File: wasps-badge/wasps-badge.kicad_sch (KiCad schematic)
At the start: 25 parts, among them J1 Conn_Debug, J2 Conn_AddOn, J3 Conn_CTF, J4 Conn_Misc, SW1 SW_SPST, SW2 SW_Push, SW3 SW_Push, U1 CH32V003FxPx

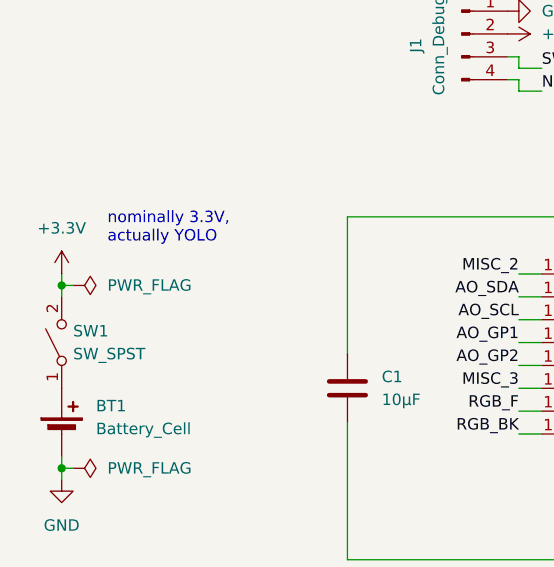
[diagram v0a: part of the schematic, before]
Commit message: Add missing footprint assignments
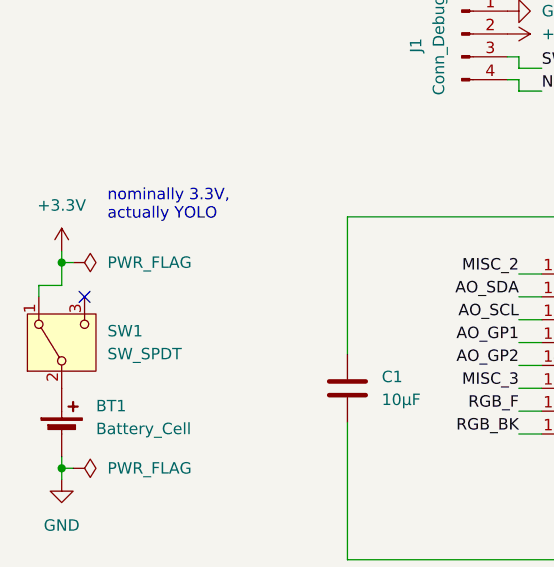
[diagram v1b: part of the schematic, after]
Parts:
- removed SW1: SW_SPST, symbol Switch:SW_SPST
- added SW1: SW_SPDT, CustomLibrary:SW_SPDT_MSS22D18_SMD, symbol Switch:SW_SPDT
- SW2, SW3: footprint (none) -> CustomLibrary:SW_PUSH_L4.0-W3.0-LS5.0_SMD
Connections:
- net +3.3V: now also SW1.1 (A)
- net at BT1.1 (+): now also SW1.2 (B)
- no-connect marks 4 -> 5
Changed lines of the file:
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@@
 	(text "nominally 3.3V,\nactually YOLO"
 		(exclude_from_sim no)
-		(at 43.18 58.42 0)
+		(at 43.18 55.88 0)
 		(effects
 			(font
@@
 	)
 	(junction
-		(at 38.1 64.77)
+		(at 38.1 62.23)
 		(diameter 0)
 		(color 0 0 0 0)
@@
 	)
 	(no_connect
+		(at 40.64 66.04)
+	)
+	(no_connect
 		(at 204.47 63.5)
 	)
@@
 	(wire
 		(pts
+			(xy 35.56 66.04) (xy 35.56 64.77)
+		)
+		(stroke
+			(width 0)
+			(type default)
+		)
+	)
+	(wire
+		(pts
 			(xy 157.48 38.1) (xy 158.75 38.1)
 		)
@@
 	(wire
 		(pts
-			(xy 38.1 64.77) (xy 38.1 66.04)
+			(xy 38.1 62.23) (xy 38.1 64.77)
 		)
 		(stroke
@@
 	(wire
 		(pts
+			(xy 35.56 64.77) (xy 38.1 64.77)
+		)
+		(stroke
+			(width 0)
+			(type default)
+		)
+	)
+	(wire
+		(pts
 			(xy 101.6 95.25) (xy 101.6 93.98)
 		)
@@
 	(wire
 		(pts
-			(xy 38.1 63.5) (xy 38.1 64.77)
+			(xy 38.1 60.96) (xy 38.1 62.23)
 		)
 		(stroke
@@
 	(wire
 		(pts
-			(xy 39.37 64.77) (xy 38.1 64.77)
+			(xy 39.37 62.23) (xy 38.1 62.23)
 		)
 		(stroke
@@
 	(symbol
 		(lib_id "power:+3.3V")
-		(at 38.1 63.5 0)
+		(at 38.1 60.96 0)
 		(unit 1)
 		(exclude_from_sim no)
@@
 		(fields_autoplaced yes)
 		(property "Reference" "#PWR04"
-			(at 38.1 67.31 0)
+			(at 38.1 64.77 0)
 			(effects
 				(font
@@
 		)
 		(property "Value" "+3.3V"
-			(at 38.1 58.42 0)
+			(at 38.1 55.88 0)
 			(effects
 				(font
@@
 		)
 		(property "Footprint" ""
-			(at 38.1 63.5 0)
+			(at 38.1 60.96 0)
 			(effects
 				(font
@@
 		)
 		(property "Datasheet" ""
-			(at 38.1 63.5 0)
+			(at 38.1 60.96 0)
 			(effects
 				(font
@@
 		)
 		(property "Description" "Power symbol creates a global label with name \"+3.3V\""
-			(at 38.1 63.5 0)
+			(at 38.1 60.96 0)
 			(effects
 				(font
@@
 	(symbol
 		(lib_id "power:PWR_FLAG")
-		(at 39.37 64.77 270)
+		(at 39.37 62.23 270)
 		(unit 1)
 		(exclude_from_sim no)
@@
 		(fields_autoplaced yes)
 		(property "Reference" "#FLG01"
-			(at 41.275 64.77 0)
+			(at 41.275 62.23 0)
 			(effects
 				(font
@@
 		)
 		(property "Value" "PWR_FLAG"
-			(at 43.18 64.7699 90)
+			(at 43.18 62.2299 90)
 			(effects
 				(font
@@
 		)
 		(property "Footprint" ""
-			(at 39.37 64.77 0)
+			(at 39.37 62.23 0)
 			(effects
 				(font
@@
 		)
 		(property "Datasheet" "~"
-			(at 39.37 64.77 0)
+			(at 39.37 62.23 0)
 			(effects
 				(font
@@
 		)
 		(property "Description" "Special symbol for telling ERC where power comes from"
-			(at 39.37 64.77 0)
+			(at 39.37 62.23 0)
 			(effects
 				(font
@@
 	)
 	(symbol
+		(lib_id "Switch:SW_SPDT")
+		(at 38.1 71.12 90)
+		(unit 1)
+		(exclude_from_sim no)
+		(in_bom yes)
+		(on_board yes)
+		(dnp no)
+		(fields_autoplaced yes)
+		(property "Reference" "SW1"
+			(at 43.18 69.8499 90)
+			(effects
+				(font
+					(size 1.27 1.27)
+				)
+				(justify right)
+			)
+		)
+		(property "Value" "SW_SPDT"
+			(at 43.18 72.3899 90)
+			(effects
+				(font
+					(size 1.27 1.27)
+				)
+				(justify right)
+			)
+		)
+		(property "Footprint" "CustomLibrary:SW_SPDT_MSS22D18_SMD"
+			(at 38.1 71.12 0)
+			(effects
+				(font
+					(size 1.27 1.27)
+				)
+				(hide yes)
+			)
+		)
+		(property "Datasheet" "~"
+			(at 45.72 71.12 0)
+			(effects
+				(font
+					(size 1.27 1.27)
+				)
+				(hide yes)
+			)
+		)
+		(property "Description" "Switch, single pole double throw"
+			(at 38.1 71.12 0)
+			(effects
+				(font
+					(size 1.27 1.27)
+				)
+				(hide yes)
+			)
+		)
+		(pin "1"
+		)
+		(pin "3"
+		)
+		(pin "2"
+		)
+		(instances
+			(project ""
+				(path "/d84c9b78-3f5c-4638-8181-576e3884c024"
+					(reference "SW1")
+					(unit 1)
+				)
+			)
+		)
+	)
+	(symbol
 		(lib_id "power:+3.3V")
 		(at 87.63 36.83 270)
@@
 			)
 		)
-		(property "Footprint" ""
+		(property "Footprint" "CustomLibrary:SW_PUSH_L4.0-W3.0-LS5.0_SMD"
 			(at 132.08 87.63 0)
 			(effects
@@
 			)
 		)
-		(property "Footprint" ""
+		(property "Footprint" "CustomLibrary:SW_PUSH_L4.0-W3.0-LS5.0_SMD"
 			(at 259.08 106.68 0)
 			(effects
@@
 					(unit 1)
 				)
-			)
-		)
-	)
-	(symbol
-		(lib_id "Switch:SW_SPST")
-		(at 38.1 71.12 90)
-		(unit 1)
-		(exclude_from_sim no)
-		(in_bom yes)
-		(on_board yes)
-		(dnp no)
-		(fields_autoplaced yes)
-		(property "Reference" "SW1"
-			(at 39.37 69.8499 90)
-			(effects
-				(font
-					(size 1.27 1.27)
-				)
-				(justify right)
-			)
-		)
-		(property "Value" "SW_SPST"
-			(at 39.37 72.3899 90)
-			(effects
-				(font
-					(size 1.27 1.27)
-				)
-				(justify right)
-			)
-		)
-		(property "Footprint" ""
-			(at 38.1 71.12 0)
-			(effects
-				(font
-					(size 1.27 1.27)
-				)
-				(hide yes)
-			)
-		)
-		(property "Datasheet" "~"
-			(at 38.1 71.12 0)
-			(effects
-				(font
-					(size 1.27 1.27)
-				)
-				(hide yes)
-			)
-		)
-		(property "Description" "Single Pole Single Throw (SPST) switch"
-			(at 38.1 71.12 0)
-			(effects
-				(font
-					(size 1.27 1.27)
-				)
-				(hide yes)
-			)
-		)
-		(pin "2"
-		)
-		(pin "1"
-		)
-		(instances
-			(project ""
-				(path "/d84c9b78-3f5c-4638-8181-576e3884c024"
-					(reference "SW1")
-					(unit 1)
-				)

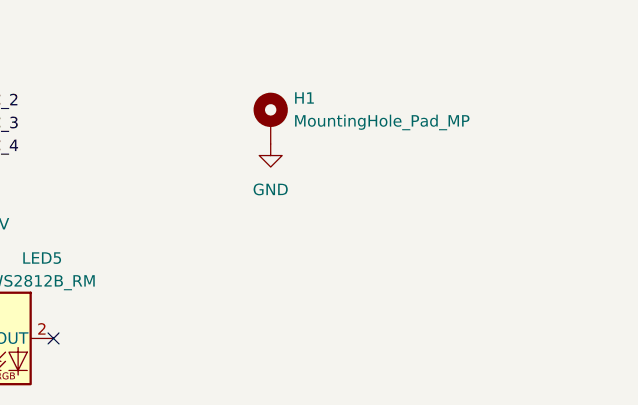
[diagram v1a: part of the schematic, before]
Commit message: Change mounting hole pad name
The footprint calls it "1", so "1" it is.
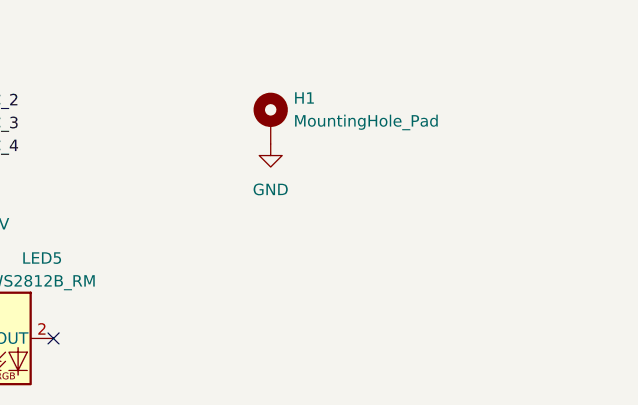
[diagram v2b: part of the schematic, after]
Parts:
- H1: value MountingHole_Pad_MP -> MountingHole_Pad; symbol Mechanical:MountingHole_Pad_MP -> Mechanical:MountingHole_Pad
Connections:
- net GND: now also H1.1; no longer H1.MP
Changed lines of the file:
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@@
 	)
 	(symbol
-		(lib_id "Mechanical:MountingHole_Pad_MP")
+		(lib_id "Mechanical:MountingHole_Pad")
 		(at 228.6 39.37 0)
 		(unit 1)
@@
 			)
 		)
-		(property "Value" "MountingHole_Pad_MP"
+		(property "Value" "MountingHole_Pad"
 			(at 231.14 39.3699 0)
 			(effects
@@
 			)
 		)
-		(property "Description" "Mounting Hole with connection as pad named MP"
+		(property "Description" "Mounting Hole with connection"
 			(at 228.6 39.37 0)
 			(effects
@@
 			)
 		)
-		(pin "MP"
+		(pin "1"
 		)
 		(instances

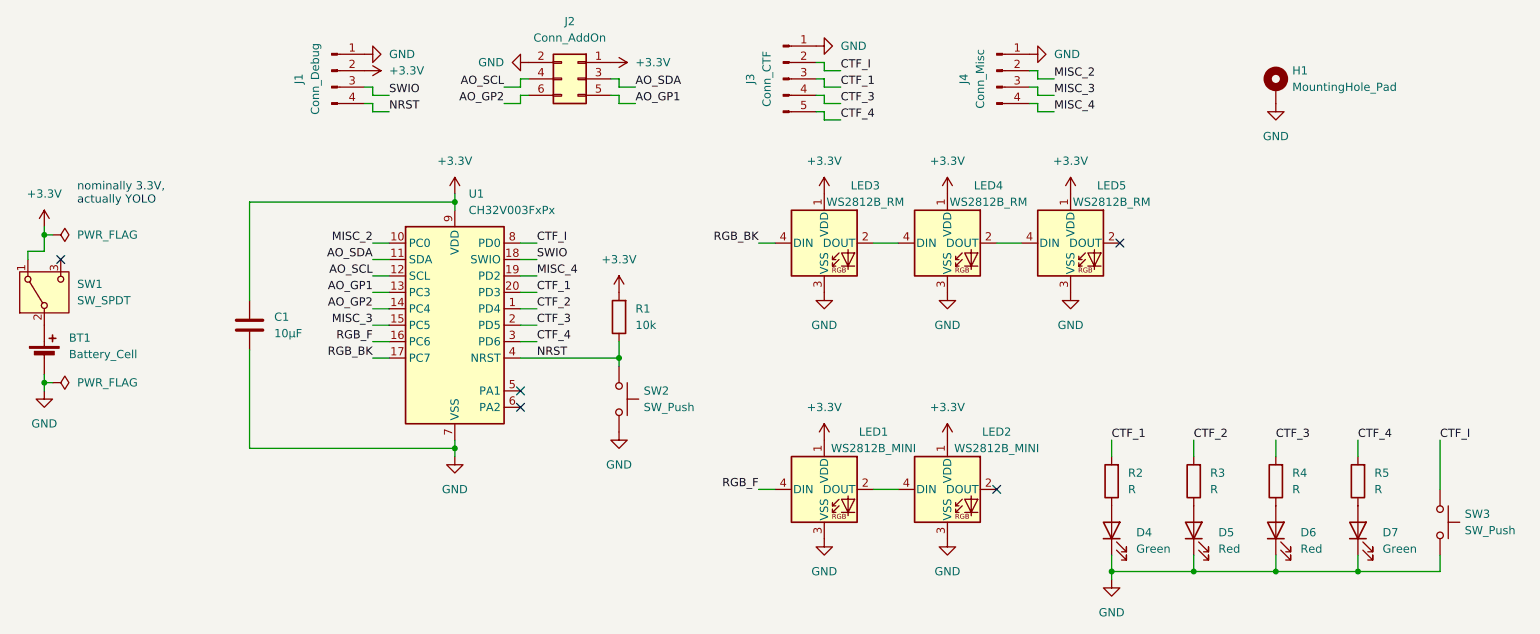
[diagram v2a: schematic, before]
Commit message: First routing attempt; drop MISC header
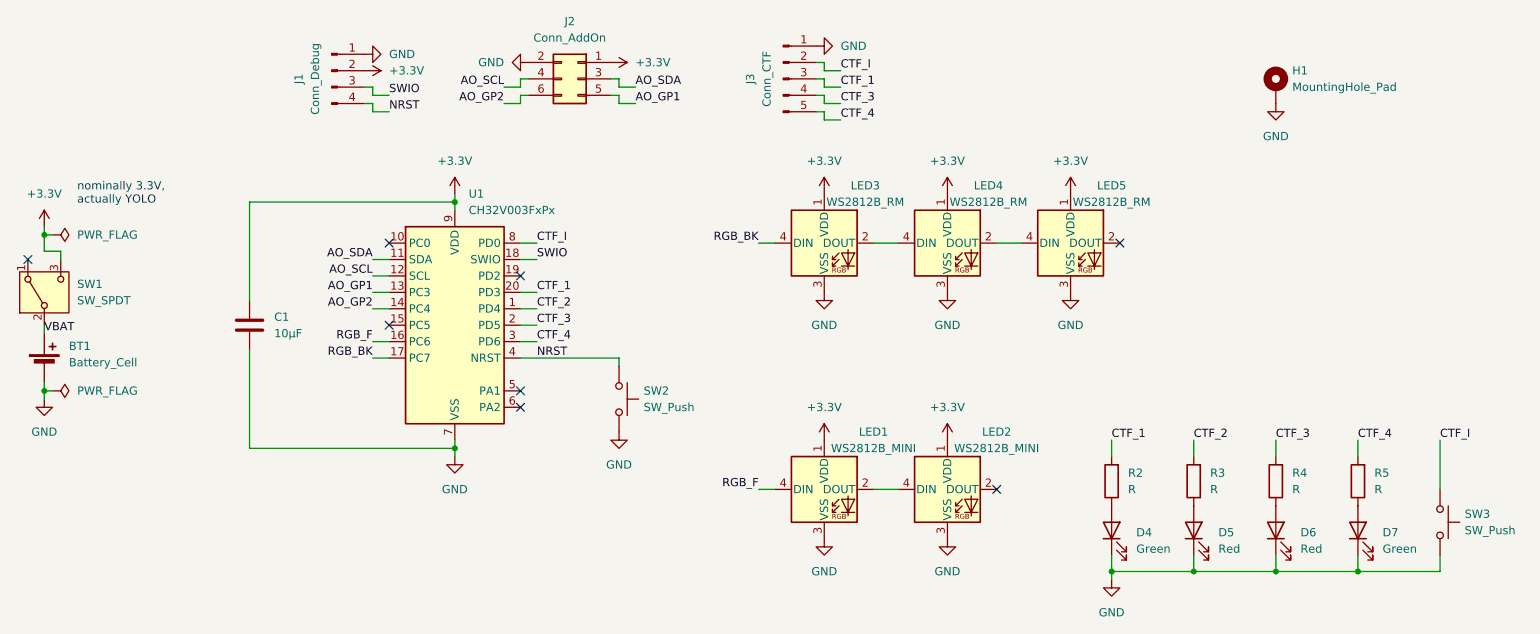
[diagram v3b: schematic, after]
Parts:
- removed J4: Conn_Misc, Connector_PinHeader_2.54mm:PinHeader_1x04_P2.54mm_Vertical, symbol Connector:Conn_01x04_Pin
- removed R1: 10k, Resistor_SMD:R_0603_1608Metric_Pad0.98x0.95mm_HandSolder, symbol Device:R
- LED3, LED4, LED5: footprint LED_SMD:LED_WS2812B_PLCC4_5.0x5.0mm_P3.2mm -> CustomLibrary:LED_WS2812B_Reverse
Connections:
- net +3.3V: now also SW1.3 (C); no longer SW1.1 (A)
- net VBAT: now reaches BT1.1 (+), SW1.2 (B)
- net MISC_2: no longer names the net of U1.10 (PC0)
- net MISC_3: no longer names the net of U1.15 (PC5)
- net MISC_4: no longer names the net of U1.19 (PD2)
- no-connect marks 5 -> 8
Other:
- moved on the sheet: BT1

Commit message: Add labeling
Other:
- company: (none) -> ${COMPANY}
- title: (none) -> ${TITLE}
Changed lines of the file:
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@@
 	(generator_version "9.0")
 	(paper "A4")
+	(title_block
+		(title "${TITLE}")
+		(date "${DATE}")
+		(rev "${REVISION}")
+		(company "${COMPANY}")
+	)
 	(text "nominally 3.3V,\nactually YOLO"
 		(exclude_from_sim no)

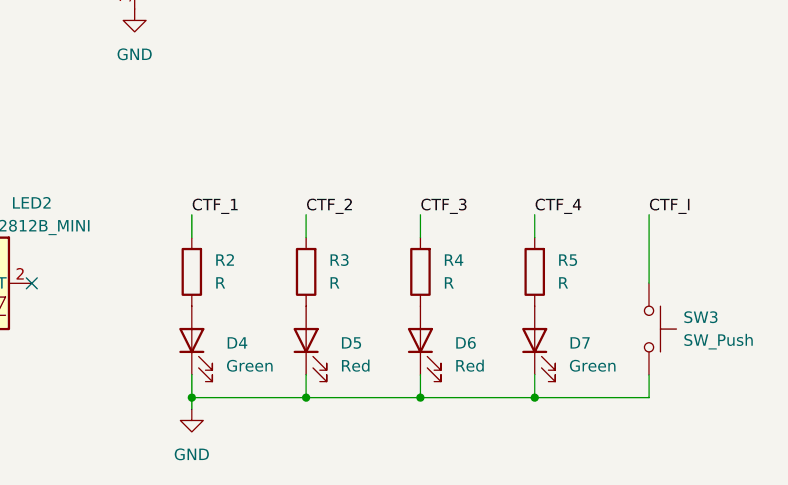
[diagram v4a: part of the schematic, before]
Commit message: Define resistor values
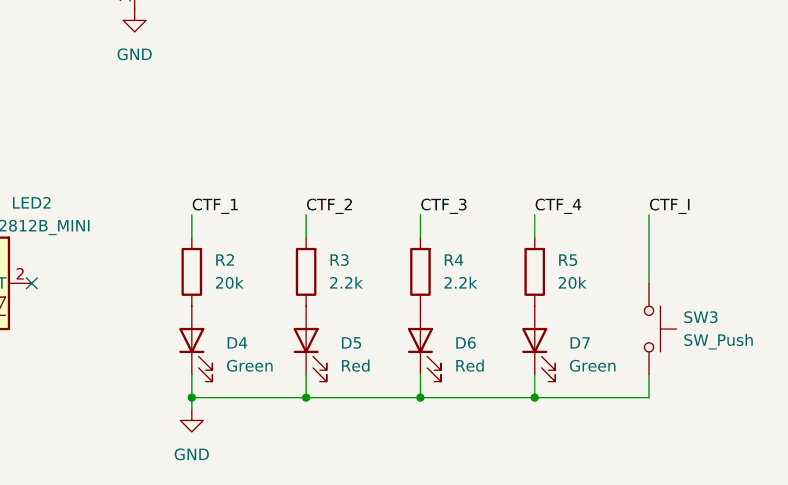
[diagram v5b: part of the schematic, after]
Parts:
- R2, R5: value R -> 20k
- R3, R4: value R -> 2.2k
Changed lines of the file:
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@@
 			)
 		)
-		(property "Value" "R"
+		(property "Value" "2.2k"
 			(at 231.14 101.5999 0)
 			(effects
@@
 			)
 		)
-		(property "Value" "R"
+		(property "Value" "20k"
 			(at 205.74 101.5999 0)
 			(effects
@@
 			)
 		)
-		(property "Value" "R"
+		(property "Value" "2.2k"
 			(at 218.44 101.5999 0)
 			(effects
@@
 			)
 		)
-		(property "Value" "R"
+		(property "Value" "20k"
 			(at 243.84 101.5999 0)
 			(effects

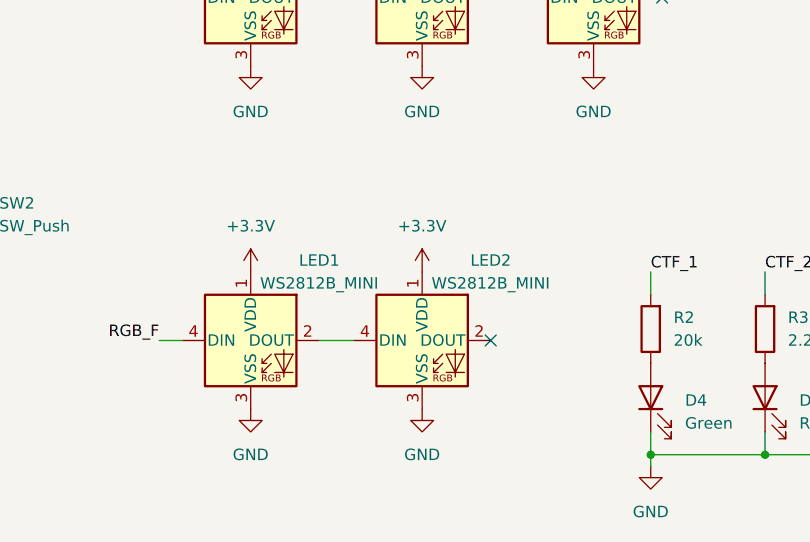
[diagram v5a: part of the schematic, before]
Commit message: Add supplier part numbers
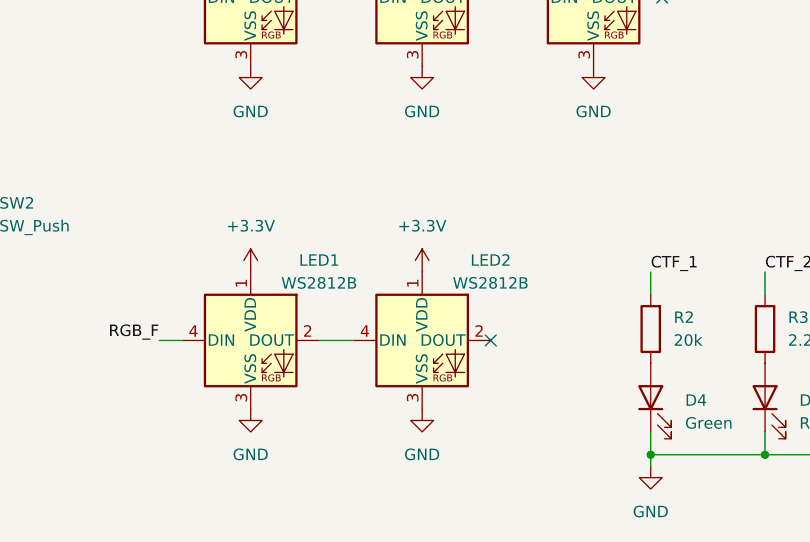
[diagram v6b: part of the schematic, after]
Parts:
- BT1: LCSC (none) -> C70377
- C1: LCSC (none) -> C19702
- D4, D7: LCSC (none) -> C12624
- D5, D6: LCSC (none) -> C965799
- J2: LCSC (none) -> C5116527
- LED1, LED2: value WS2812B_MINI -> WS2812B
- R2, R5: LCSC (none) -> C4184
- R3, R4: LCSC (none) -> C4190
- SW1: LCSC (none) -> C41375971
- SW2, SW3: LCSC (none) -> C5221275
- U1: LCSC (none) -> C5187096
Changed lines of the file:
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@@
+			)
+		)
+		(property "LCSC" "C12624"
+			(at 207.01 108.2674 0)
+			(effects
+				(font
+					(size 1.27 1.27)
+				)
+				(hide yes)
 			)
 		)
@@
 			)
 		)
+		(property "LCSC" "C41375971"
+			(at 38.1 71.12 90)
+			(effects
+				(font
+					(size 1.27 1.27)
+				)
+				(hide yes)
+			)
+		)
 		(pin "1"
 		)
@@
 			)
 		)
-		(property "Value" "WS2812B_MINI"
+		(property "Value" "WS2812B"
 			(at 166.37 95.25 0)
 			(effects
@@
 			)
 		)
+		(property "LCSC" "C70377"
+			(at 41.91 79.4384 0)
+			(effects
+				(font
+					(size 1.27 1.27)
+				)
+				(hide yes)
+			)
+		)
 		(pin "1"
 		)
@@
 		(property "Description" "Resistor"
 			(at 228.6 100.33 0)
+			(effects
+				(font
+					(size 1.27 1.27)
+				)
+				(hide yes)
+			)
+		)
+		(property "LCSC" "C4190"
+			(at 231.14 99.0599 0)
 			(effects
 				(font
@@
 			)
 		)
+		(property "LCSC" "C965799"
+			(at 232.41 108.2674 0)
+			(effects
+				(font
+					(size 1.27 1.27)
+				)
+				(hide yes)
+			)
+		)
 		(pin "2"
 		)
@@
 			)
 		)
+		(property "LCSC" "C965799"
+			(at 219.71 108.2674 0)
+			(effects
+				(font
+					(size 1.27 1.27)
+				)
+				(hide yes)
+			)
+		)
 		(pin "2"
 		)
@@
 			)
 		)
+		(property "LCSC" "C4184"
+			(at 205.74 99.0599 0)
+			(effects
+				(font
+					(size 1.27 1.27)
+				)
+				(hide yes)
+			)
+		)
 		(pin "1"
 		)
@@
 			)
 		)
-		(property "Value" "WS2812B_MINI"
+		(property "Value" "WS2812B"
 			(at 185.42 95.25 0)
 			(effects
@@
 			)
 		)
+		(property "LCSC" "C12624"
+			(at 245.11 108.2674 0)
+			(effects
+				(font
+					(size 1.27 1.27)
+				)
+				(hide yes)
+			)
+		)
 		(pin "2"
 		)
@@
 			)
 		)
+		(property "LCSC" "C5221275"
+			(at 130.81 86.3599 0)
+			(effects
+				(font
+					(size 1.27 1.27)
+				)
+				(hide yes)
+			)
+		)
 		(pin "2"
 		)
@@
 		(property "Description" "Push button switch, generic, two pins"
 			(at 254 106.68 0)
+			(effects
+				(font
+					(size 1.27 1.27)
+				)
+				(hide yes)
+			)
+		)
+		(property "LCSC" "C5221275"
+			(at 257.81 105.4099 0)
 			(effects
 				(font
@@
 			)
 		)
+		(property "LCSC" "C19702"
+			(at 73.66 74.9299 0)
+			(effects
+				(font
+					(size 1.27 1.27)
+				)
+				(hide yes)
+			)
+		)
 		(pin "2"
 		)
@@
 			)
 		)
+		(property "LCSC" "C5116527"
+			(at 119.38 29.21 0)
+			(effects
+				(font
+					(size 1.27 1.27)
+				)
+				(hide yes)
+			)
+		)
 		(pin "3"
 		)
@@
 			)
 		)
+		(property "LCSC" "C4190"
+			(at 218.44 99.0599 0)
+			(effects
+				(font
+					(size 1.27 1.27)
+				)
+				(hide yes)
+			)
+		)
 		(pin "1"
 		)
@@
 			)
 		)
+		(property "LCSC" "C5187096"
+			(at 103.7433 55.88 0)
+			(effects
+				(font
+					(size 1.27 1.27)
+				)
+				(hide yes)
+			)
+		)
 		(pin "19"
 		)
@@
 			(effects
 				(font
+					(size 1.27 1.27)
+				)
+				(hide yes)
+			)
+		)
+		(property "LCSC" "C4184"
+			(at 243.84 99.0599 0)
+			(effects
+				(font
